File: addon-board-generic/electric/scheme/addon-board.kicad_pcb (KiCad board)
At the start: 2 copper layers, 85 x 56 mm, 66 parts, among them K1 CONN_3, K2 CONN_3, K3 CONN_3, K4 CONN_3, K5 CONN_3, K6 CONN_3, K7 CONN_3, K8 CONN_3, P1 TST, P10 CONN_8, P11 CONN_10, P12 CONN_4, P13 CONN_4, P2 TST, P3 cross board conn, P4 cross board conn, P5 TST, P6 TST, P7 TST, P8 TST, P9 CONN_4, Q1 NPN, Q2 MOS_P, Q3 BC847, Q4 BC847, Q5 MOS_P, Q6 MOS_P, U1 L293, U2 L293, U3 74HC165, U4 74HC595_MY, U5 74HC595_MY, X1 8MHz

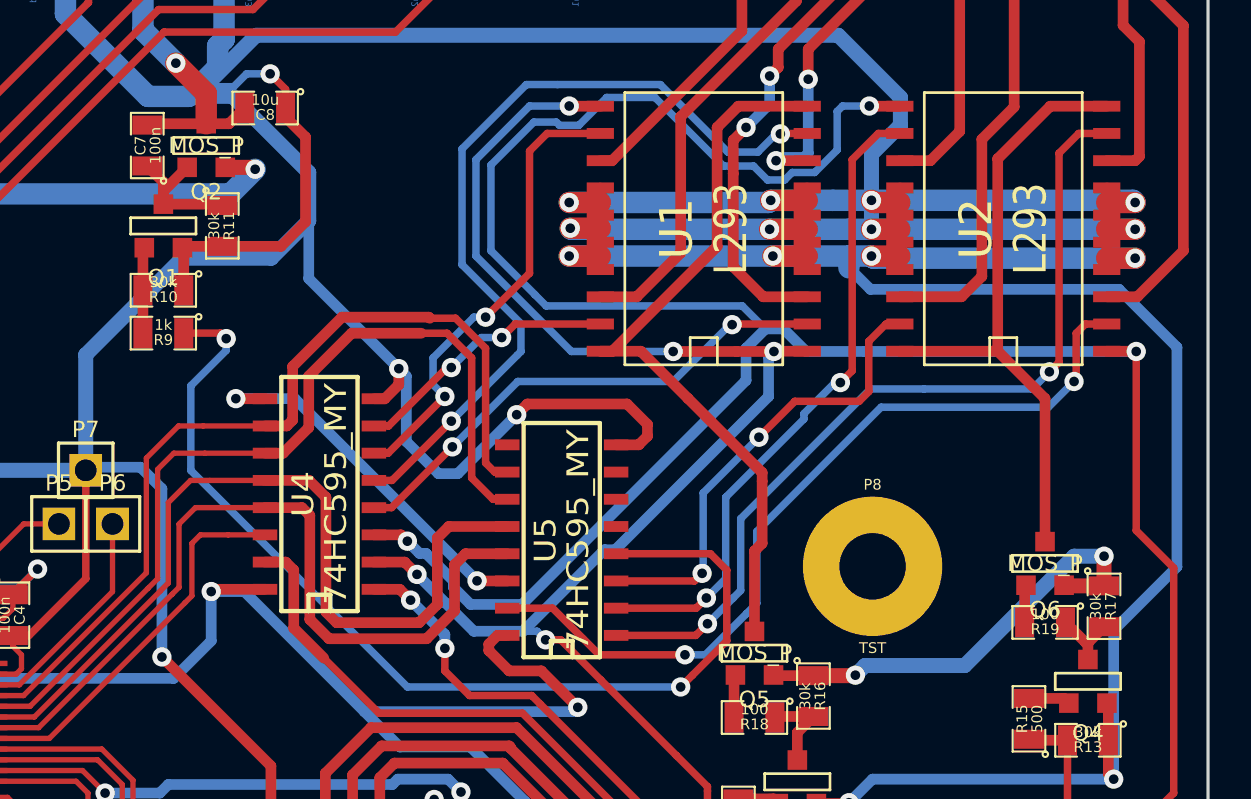
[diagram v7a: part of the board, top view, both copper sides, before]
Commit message: Raplaced power mosfets with sot23 transistors because of their max current and very low resistance.
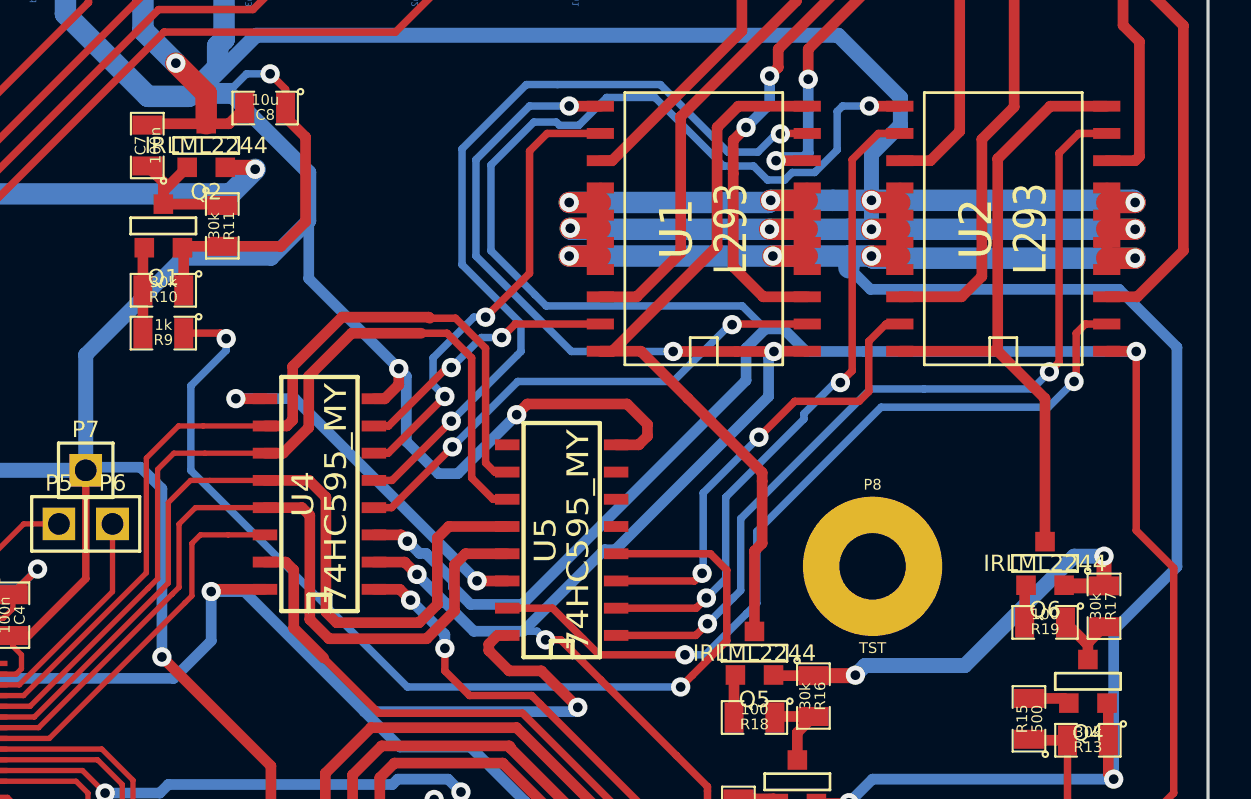
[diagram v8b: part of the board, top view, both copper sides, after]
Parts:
- Q2, Q5, Q6: value MOS_P -> IRLML2244
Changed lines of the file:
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@@
     (links 205)
     (no_connects 0)
-    (area 127.606667 112.000001 228.575001 181.9116)
+    (area 127.606667 112.000001 228.575001 182.5466)
     (thickness 1.6)
     (drawings 49)
@@
   )
   (setup
-    (last_trace_width 0.7)
+    (last_trace_width 0.25)
     (user_trace_width 0.35)
     (user_trace_width 0.5)
@@
       (effects (font (size 0.762 0.762) (thickness 0.12954)))
     )
-    (fp_text value MOS_P (at 0 0 180) (layer F.SilkS)
+    (fp_text value IRLML2244 (at 0 0 180) (layer F.SilkS)
       (effects (font (size 0.762 0.762) (thickness 0.12954)))
     )
@@
       (effects (font (size 0.762 0.762) (thickness 0.12954)))
     )
-    (fp_text value MOS_P (at 0 0 180) (layer F.SilkS)
+    (fp_text value IRLML2244 (at 0 0 180) (layer F.SilkS)
       (effects (font (size 0.762 0.762) (thickness 0.12954)))
     )
@@
       (effects (font (size 0.762 0.762) (thickness 0.12954)))
     )
-    (fp_text value MOS_P (at 0 0 180) (layer F.SilkS)
-      (effects (font (size 0.762 0.762) (thickness 0.12954)))
-    )
+    (fp_text value IRLML2244 (at 0 0 180) (layer F.SilkS)
+      (effects (font (size 0.762 0.762) (thickness 0.12954)))
+    )
